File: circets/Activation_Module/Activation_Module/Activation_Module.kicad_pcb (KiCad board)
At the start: 2 copper layers, 50 parts, among them J1 Bus_Connector, J2 To_Bus, J3 From_Bus, J4 Mode_R, J5 Mode_W, J6 Enable Connector, SW1 SW_DIP_x04, SW2 SW_DIP_x04, U1 74HC541, U10 74HC541, U11 74HC00, U12 74HC541, U13 74HC541, U14 74HC541, U15 74LS86, U16 74LS86, U17 74LS32, U18 74LS32, U19 74157, U2 74HC541, U20 74157, U3 74LS86, U4 74LS86, U5 74LS32, U6 74LS32, U7 74HC541, U8 74HC541, U9 74HC00

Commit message: Started Creating Activation Module PCB
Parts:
- removed J3: From_Bus, Connector_PinHeader_2.54mm:PinHeader_1x16_P2.54mm_Vertical
- removed J4: Mode_R, Connector_PinSocket_2.54mm:PinSocket_1x03_P2.54mm_Vertical
- removed J5: Mode_W, Connector_PinSocket_2.54mm:PinSocket_1x03_P2.54mm_Vertical
- removed J6: Enable Connector, Connector_PinSocket_2.54mm:PinSocket_1x03_P2.54mm_Vertical
- added C7: 0.1µF, Capacitor_THT:C_Disc_D6.0mm_W2.5mm_P5.00mm, F.Cu at (-340.9, 76.1)
- added C8: 0.1µF, Capacitor_THT:C_Disc_D6.0mm_W2.5mm_P5.00mm, F.Cu at (-389.8, 80.2)
- added U21: 74157, Package_DIP:DIP-16_W7.62mm_Socket, F.Cu at (-318.4, 29.6)
- added U22: 74LS32, Package_DIP:DIP-14_W7.62mm_Socket, F.Cu at (-294.9, 29.6)
- added U23: 74LS00, Package_DIP:DIP-14_W7.62mm_Socket, F.Cu at (-365.4, 56.7)
- J1: footprint Computer_Component_Library:BusConnector -> Computer_Component_Library:PinSocket_1x78_P2.00mm_Horizontal
- J2: value To_Bus -> Conn_01x03_Male; footprint Connector_PinHeader_2.54mm:PinHeader_1x16_P2.54mm_Vertical -> Connector_PinSocket_2.00mm:PinSocket_1x03_P2.00mm_Vertical
- R10, R9: value 220 -> 1k
- R5, R6: value 1k -> 220
- U1, U10, U14, U8: footprint Computer_Component_Library:74HC541-PDIP -> Package_DIP:DIP-20_W7.62mm_Socket
- U11, U9: value 74HC00 -> 74HC541; footprint Package_DIP:DIP-14_W7.62mm_Socket -> Package_DIP:DIP-20_W7.62mm_Socket
- U12, U13: value 74HC541 -> 74LS86; footprint Computer_Component_Library:74HC541-PDIP -> Package_DIP:DIP-14_W7.62mm_Socket
- U15, U16: value 74LS86 -> 74LS32
- U17: value 74LS32 -> 74HC541; footprint Package_DIP:DIP-14_W7.62mm_Socket -> Package_DIP:DIP-20_W7.62mm_Socket
- U18: value 74LS32 -> 74HC00
- U19: value 74157 -> 74LS08; footprint Package_DIP:DIP-16_W7.62mm_Socket -> Package_DIP:DIP-14_W7.62mm_Socket
- U2: value 74HC541 -> AM-Connector; footprint Computer_Component_Library:74HC541-PDIP -> Computer_Component_Library:PinSocket_1x42_P2.00mm_Horizontal
- U3: value 74LS86 -> 74HC541; footprint Package_DIP:DIP-14_W7.62mm_Socket -> Package_DIP:DIP-20_W7.62mm_Socket
- U5: value 74LS32 -> 74LS86
- U7: value 74HC541 -> 74LS32; footprint Computer_Component_Library:74HC541-PDIP -> Package_DIP:DIP-14_W7.62mm_Socket
- moved C6 577.0 mm to (-349.0, 76.1), turned to 0 degrees
- moved R9 520.7 mm to (-377.1, 90.8), turned to 0 degrees
- moved R10 517.4 mm to (-370.9, 90.8), turned to 0 degrees
- moved R11 514.8 mm to (-364.8, 90.8), turned to 0 degrees
- moved D2 511.7 mm to (-377.2, 81.4)
- moved R12 509.4 mm to (-351.1, 80.2), turned to 0 degrees
- moved D4 508.1 mm to (-364.2, 81.4)
- moved D3 506.1 mm to (-370.7, 81.4)
- moved U15 505.3 mm to (-400.7, 56.7), turned to 0 degrees
- moved C3 496.6 mm to (-373.5, 76.1)
- moved C4 489.6 mm to (-365.3, 76.1), turned to 0 degrees
- moved D1 488.1 mm to (-357.7, 81.4)
- moved U16 484.5 mm to (-377.7, 33.6), turned to 0 degrees
- moved C5 477.0 mm to (-357.2, 76.1), turned to 0 degrees
- moved U4 466.7 mm to (-353.7, 56.7), turned to 0 degrees
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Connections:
- D1 pad 1: Net-(D1-Pad1) -> /~WE1
- D2 pad 1: Net-(D2-Pad1) -> /~WE2
- D3 pad 1: Net-(D3-Pad1) -> /~RE1
- D4 pad 1: Net-(D4-Pad1) -> /~RE2
- J1 pad 37: Net-(J1-Pad37) -> /WE1:0
- J1 pad 38: Net-(J1-Pad38) -> /WE1:1
- J1 pad 39: Net-(J1-Pad39) -> /WE1:2
- J1 pad 40: Net-(J1-Pad40) -> /WE1:3
- J1 pad 41: Net-(J1-Pad41) -> /WE1:4
- J1 pad 42: Net-(J1-Pad42) -> /WE1:5
- J1 pad 43: Net-(J1-Pad43) -> /WE1:6
- J1 pad 44: Net-(J1-Pad44) -> /WE2:0
- J1 pad 45: Net-(J1-Pad45) -> /WE2:1
- J1 pad 46: Net-(J1-Pad46) -> /WE2:2
- J1 pad 47: Net-(J1-Pad47) -> /WE2:3
- J1 pad 48: Net-(J1-Pad48) -> /WE2:4
- J1 pad 49: Net-(J1-Pad49) -> /WE2:5
- J1 pad 50: Net-(J1-Pad50) -> /WE2:6
- J1 pad 51: Net-(J1-Pad51) -> /RE1:0
- J1 pad 52: Net-(J1-Pad52) -> /RE1:1
- J1 pad 53: Net-(J1-Pad53) -> /RE1:2
- J1 pad 54: Net-(J1-Pad54) -> /RE1:3
- J1 pad 55: Net-(J1-Pad55) -> /RE1:4
- J1 pad 56: Net-(J1-Pad56) -> /RE1:5
- J1 pad 57: Net-(J1-Pad57) -> /RE1:6
- J1 pad 58: Net-(J1-Pad58) -> /RE2:0
- J1 pad 59: Net-(J1-Pad59) -> /RE2:1
- J1 pad 60: Net-(J1-Pad60) -> /RE2:2
- J1 pad 61: Net-(J1-Pad61) -> /RE2:3
- J1 pad 62: Net-(J1-Pad62) -> /RE2:4
- J1 pad 63: Net-(J1-Pad63) -> /RE2:5
- J1 pad 64: Net-(J1-Pad64) -> /RE2:6
- J1 pad 65: (no net) -> Net-(J1-Pad65)
- J1 pad 66: (no net) -> Net-(J1-Pad66)
- J1 pad 67: (no net) -> Net-(J1-Pad67)
- J2 pad 2: Net-(J2-Pad2) -> /~SUP
- J2 pad 3: Net-(J2-Pad3) -> GND
- R10 pad 1: +5V -> GND
- R10 pad 2: Net-(D2-Pad2) -> Net-(R10-Pad2)
- R5 pad 1: GND -> +5V
- R5 pad 2: Net-(R5-Pad2) -> Net-(D1-Pad2)
- R6 pad 1: GND -> +5V
- R6 pad 2: Net-(R6-Pad2) -> Net-(D2-Pad2)
- R9 pad 1: +5V -> GND
- R9 pad 2: Net-(D1-Pad2) -> Net-(R9-Pad2)
- SW2 pad 5: Net-(R8-Pad2) -> Net-(R10-Pad2)
- SW2 pad 6: Net-(R7-Pad2) -> Net-(R9-Pad2)
- SW2 pad 7: Net-(R6-Pad2) -> Net-(R8-Pad2)
- SW2 pad 8: Net-(R5-Pad2) -> Net-(R7-Pad2)
- U1 pad 1: Net-(D3-Pad1) -> /~RE1
- U1 pad 2: Net-(J2-Pad1) -> Net-(U1-Pad2)
- U1 pad 3: Net-(J2-Pad2) -> Net-(U1-Pad3)
- U1 pad 4: Net-(J2-Pad3) -> Net-(U1-Pad4)
- U1 pad 5: Net-(J2-Pad4) -> Net-(U1-Pad5)
- U1 pad 6: Net-(J2-Pad5) -> Net-(U1-Pad6)
- U1 pad 7: Net-(J2-Pad6) -> Net-(U1-Pad7)
- U1 pad 8: Net-(J2-Pad7) -> Net-(U1-Pad8)
- U1 pad 9: Net-(J2-Pad8) -> Net-(U1-Pad9)
- U10 pad 1: Net-(D4-Pad1) -> /~RE2
- U10 pad 2: Net-(J2-Pad1) -> Net-(U1-Pad2)
- U10 pad 3: Net-(J2-Pad2) -> Net-(U1-Pad3)
- U10 pad 4: Net-(J2-Pad3) -> Net-(U1-Pad4)
- U10 pad 5: Net-(J2-Pad4) -> Net-(U1-Pad5)
- U10 pad 6: Net-(J2-Pad5) -> Net-(U1-Pad6)
- U10 pad 7: Net-(J2-Pad6) -> Net-(U1-Pad7)
- U10 pad 8: Net-(J2-Pad7) -> Net-(U1-Pad8)
- U10 pad 9: Net-(J2-Pad8) -> Net-(U1-Pad9)
- U11 pad 1: Net-(U11-Pad1) -> /~RE2
- U11 pad 10: Net-(U11-Pad10) -> GND
- U11 pad 11: Net-(U11-Pad11) -> Net-(J1-Pad36)
- U11 pad 12: Net-(U11-Pad12) -> Net-(J1-Pad35)
- U11 pad 13: Net-(U11-Pad13) -> Net-(J1-Pad34)
- U11 pad 14: +5V -> Net-(J1-Pad33)
- U11 pad 2: Net-(U11-Pad1) -> Net-(U11-Pad2)
- U11 pad 7: GND -> Net-(U11-Pad7)
- U12 pad 1: Net-(D4-Pad1) -> Net-(R7-Pad2)
- U12 pad 10: GND -> /RE1:5
- U12 pad 11: Net-(J1-Pad36) -> Net-(U12-Pad11)
- U12 pad 12: Net-(J1-Pad35) -> Net-(R10-Pad2)
- U12 pad 13: Net-(J1-Pad34) -> /RE1:6
- U12 pad 14: Net-(J1-Pad33) -> +5V
- U12 pad 2: Net-(J2-Pad9) -> /RE1:3
- U12 pad 3: Net-(J2-Pad10) -> Net-(U12-Pad3)
- U12 pad 4: Net-(J2-Pad11) -> Net-(R8-Pad2)
- U12 pad 5: Net-(J2-Pad12) -> /RE1:4
- U12 pad 6: Net-(J2-Pad13) -> Net-(U12-Pad6)
- U12 pad 7: Net-(J2-Pad14) -> GND
- U12 pad 8: Net-(J2-Pad15) -> Net-(U12-Pad8)
- U12 pad 9: Net-(J2-Pad16) -> Net-(R9-Pad2)
- U13 pad 1: GND -> Net-(R7-Pad2)
- U13 pad 10: GND -> /RE2:5
- U13 pad 11: Net-(J3-Pad8) -> Net-(U13-Pad11)
- U13 pad 12: Net-(J3-Pad7) -> Net-(R10-Pad2)
- U13 pad 13: Net-(J3-Pad6) -> /RE2:6
- U13 pad 14: Net-(J3-Pad5) -> +5V
- U13 pad 2: Net-(J1-Pad21) -> /RE2:3
- U13 pad 3: Net-(J1-Pad22) -> Net-(U13-Pad3)
- U13 pad 4: Net-(J1-Pad23) -> Net-(R8-Pad2)
- U13 pad 5: Net-(J1-Pad24) -> /RE2:4
- U13 pad 6: Net-(J1-Pad25) -> Net-(U13-Pad6)
- U13 pad 7: Net-(J1-Pad26) -> GND
- U13 pad 8: Net-(J1-Pad27) -> Net-(U13-Pad8)
- U13 pad 9: Net-(J1-Pad28) -> Net-(R9-Pad2)
- U14 pad 11: Net-(J3-Pad16) -> Net-(U14-Pad11)
- U14 pad 12: Net-(J3-Pad15) -> Net-(U14-Pad12)
- U14 pad 13: Net-(J3-Pad14) -> Net-(U14-Pad13)
- U14 pad 14: Net-(J3-Pad13) -> Net-(U14-Pad14)
- U14 pad 15: Net-(J3-Pad12) -> Net-(U14-Pad15)
- U14 pad 16: Net-(J3-Pad11) -> Net-(U14-Pad16)
- U14 pad 17: Net-(J3-Pad10) -> Net-(U14-Pad17)
- U14 pad 18: Net-(J3-Pad9) -> Net-(U14-Pad18)
- U14 pad 19: Net-(D2-Pad1) -> /~WE2
- U14 pad 2: Net-(J1-Pad29) -> Net-(J1-Pad21)
- U14 pad 3: Net-(J1-Pad30) -> Net-(J1-Pad22)
- U14 pad 4: Net-(J1-Pad31) -> Net-(J1-Pad23)
- U14 pad 5: Net-(J1-Pad32) -> Net-(J1-Pad24)
- U14 pad 6: Net-(J1-Pad33) -> Net-(J1-Pad25)
- U14 pad 7: Net-(J1-Pad34) -> Net-(J1-Pad26)
- U14 pad 8: Net-(J1-Pad35) -> Net-(J1-Pad27)
- U14 pad 9: Net-(J1-Pad36) -> Net-(J1-Pad28)
- U15 pad 1: Net-(R5-Pad2) -> Net-(U12-Pad3)
- U15 pad 10: Net-(J1-Pad56) -> Net-(U15-Pad10)
- U15 pad 11: Net-(U15-Pad11) -> (no net)
- U15 pad 12: Net-(R8-Pad2) -> (no net)
- U15 pad 13: Net-(J1-Pad57) -> (no net)
- U15 pad 2: Net-(J1-Pad54) -> Net-(U12-Pad6)
- U15 pad 4: Net-(R6-Pad2) -> Net-(U13-Pad8)
- U15 pad 5: Net-(J1-Pad55) -> Net-(U13-Pad11)
- U15 pad 6: Net-(U15-Pad6) -> Net-(U15-Pad10)
- U15 pad 9: Net-(R7-Pad2) -> Net-(U15-Pad9)
- U16 pad 1: Net-(R5-Pad2) -> Net-(U13-Pad3)
- U16 pad 10: Net-(J1-Pad49) -> Net-(U12-Pad11)
- U16 pad 11: Net-(U16-Pad11) -> (no net)
- U16 pad 12: Net-(R8-Pad2) -> (no net)
- U16 pad 13: Net-(J1-Pad50) -> (no net)
- U16 pad 2: Net-(J1-Pad47) -> Net-(U13-Pad6)
- U16 pad 3: Net-(U16-Pad3) -> Net-(U15-Pad9)
- U16 pad 4: Net-(R6-Pad2) -> Net-(U15-Pad3)
- U16 pad 5: Net-(J1-Pad48) -> Net-(U16-Pad5)
- U16 pad 8: Net-(U16-Pad8) -> Net-(U16-Pad5)
- U16 pad 9: Net-(R7-Pad2) -> Net-(U12-Pad8)
- U17 pad 1: Net-(U16-Pad3) -> GND
- U17 pad 10: Net-(U17-Pad10) -> GND
- U17 pad 14: +5V -> Net-(U17-Pad14)
- U17 pad 2: Net-(U16-Pad6) -> Net-(J1-Pad29)
- U17 pad 3: Net-(U17-Pad3) -> Net-(J1-Pad30)
- U17 pad 4: Net-(U16-Pad8) -> Net-(J1-Pad31)
- U17 pad 5: Net-(U16-Pad11) -> Net-(J1-Pad32)
- U17 pad 6: Net-(U17-Pad10) -> Net-(J1-Pad33)
- U17 pad 7: GND -> Net-(J1-Pad34)
- U17 pad 8: Net-(D4-Pad1) -> Net-(J1-Pad35)
- U17 pad 9: Net-(U17-Pad3) -> Net-(J1-Pad36)
- U18 pad 1: Net-(U15-Pad3) -> Net-(U18-Pad1)
- U18 pad 10: Net-(U15-Pad11) -> Net-(U18-Pad10)
- U18 pad 11: /RE -> (no net)
- U18 pad 12: Net-(D3-Pad1) -> (no net)
- U18 pad 13: Net-(D4-Pad1) -> (no net)
- U18 pad 2: Net-(U15-Pad6) -> Net-(U18-Pad1)
- U18 pad 4: Net-(U18-Pad3) -> (no net)
- U18 pad 5: Net-(U15-Pad8) -> (no net)
- U18 pad 6: Net-(U18-Pad6) -> (no net)
- U18 pad 8: Net-(D3-Pad1) -> Net-(U18-Pad8)
- U18 pad 9: Net-(U18-Pad6) -> Net-(U18-Pad10)
- U19 pad 1: Net-(D3-Pad1) -> Net-(U18-Pad3)
- U19 pad 10: Net-(U19-Pad10) -> (no net)
- U19 pad 11: Net-(U19-Pad11) -> (no net)
- U19 pad 12: Net-(J4-Pad3) -> (no net)
- U19 pad 13: Net-(J1-Pad46) -> (no net)
- U19 pad 14: Net-(J1-Pad60) -> GND
- U19 pad 2: Net-(J1-Pad58) -> Net-(J1-Pad4)
- U19 pad 3: Net-(J1-Pad44) -> /WE_F
- U19 pad 4: Net-(J4-Pad1) -> Net-(U18-Pad3)
- U19 pad 5: Net-(J1-Pad59) -> Net-(J1-Pad3)
- U19 pad 6: Net-(J1-Pad45) -> /WE_R
- U19 pad 7: Net-(J4-Pad2) -> +5V
- U19 pad 8: GND -> (no net)
- U19 pad 9: Net-(U19-Pad9) -> (no net)
- U2 pad 1: Net-(D3-Pad1) -> Net-(U2-Pad1)
- U2 pad 10: GND -> Net-(U18-Pad8)
- U2 pad 11: Net-(J1-Pad20) -> Net-(U14-Pad18)
- U2 pad 12: Net-(J1-Pad19) -> Net-(U14-Pad17)
- U2 pad 13: Net-(J1-Pad18) -> Net-(U14-Pad16)
- U2 pad 14: Net-(J1-Pad17) -> Net-(U14-Pad15)
- U2 pad 15: Net-(J1-Pad16) -> Net-(U14-Pad14)
- U2 pad 16: Net-(J1-Pad15) -> Net-(U14-Pad13)
- U2 pad 17: Net-(J1-Pad14) -> Net-(U14-Pad12)
- U2 pad 18: Net-(J1-Pad13) -> Net-(U14-Pad11)
- U2 pad 19: GND -> Net-(U17-Pad18)
- U2 pad 2: Net-(J2-Pad9) -> Net-(U2-Pad2)
- U2 pad 20: +5V -> Net-(U17-Pad17)
- U2 pad 3: Net-(J2-Pad10) -> Net-(U2-Pad3)
- U2 pad 4: Net-(J2-Pad11) -> Net-(U2-Pad4)
- U2 pad 5: Net-(J2-Pad12) -> Net-(U2-Pad5)
- U2 pad 6: Net-(J2-Pad13) -> Net-(U2-Pad6)
- U2 pad 7: Net-(J2-Pad14) -> /WE_R
- U2 pad 8: Net-(J2-Pad15) -> /WE_F
- U2 pad 9: Net-(J2-Pad16) -> Net-(U18-Pad3)
- U20 pad 1: Net-(D1-Pad1) -> /~RE1
- U20 pad 12: Net-(J5-Pad3) -> Net-(U2-Pad3)
- U20 pad 13: Net-(J1-Pad53) -> /RE2:2
- U20 pad 14: Net-(J1-Pad39) -> /RE1:2
- U20 pad 2: Net-(J1-Pad37) -> /RE1:0
- U20 pad 3: Net-(J1-Pad51) -> /RE2:0
- U20 pad 4: Net-(J5-Pad1) -> Net-(U2-Pad1)
- U20 pad 5: Net-(J1-Pad38) -> /RE1:1
- U20 pad 6: Net-(J1-Pad52) -> /RE2:1
- U20 pad 7: Net-(J5-Pad2) -> Net-(U2-Pad2)
- U3 pad 1: Net-(R1-Pad2) -> /~RE1
- U3 pad 10: Net-(J1-Pad42) -> GND
- U3 pad 11: Net-(U3-Pad11) -> Net-(J1-Pad20)
- U3 pad 12: Net-(R4-Pad2) -> Net-(J1-Pad19)
- U3 pad 13: Net-(J1-Pad43) -> Net-(J1-Pad18)
- U3 pad 14: GND -> Net-(J1-Pad17)
- U3 pad 2: Net-(J1-Pad40) -> Net-(U11-Pad2)
- U3 pad 3: Net-(U3-Pad3) -> Net-(U11-Pad3)
- U3 pad 4: Net-(R2-Pad2) -> Net-(U11-Pad4)
- U3 pad 5: Net-(J1-Pad41) -> Net-(U11-Pad5)
- U3 pad 6: Net-(U3-Pad6) -> Net-(U11-Pad6)
- U3 pad 7: +5V -> Net-(U11-Pad7)
- U3 pad 8: Net-(U3-Pad8) -> Net-(U11-Pad8)
- U3 pad 9: Net-(R3-Pad2) -> Net-(U11-Pad9)
- U4 pad 10: Net-(J1-Pad63) -> /WE1:5
- U4 pad 13: Net-(J1-Pad64) -> /WE1:6
- U4 pad 14: +5V -> GND
- U4 pad 2: Net-(J1-Pad61) -> /WE1:3
- U4 pad 5: Net-(J1-Pad62) -> /WE1:4
- U4 pad 7: GND -> +5V
- U5 pad 1: Net-(U3-Pad3) -> Net-(R1-Pad2)
- U5 pad 10: Net-(U3-Pad11) -> /WE2:5
- U5 pad 11: Net-(U11-Pad1) -> Net-(U5-Pad11)
- U5 pad 12: Net-(D1-Pad1) -> Net-(R4-Pad2)
- U5 pad 13: Net-(D2-Pad1) -> /WE2:6
- U5 pad 2: Net-(U3-Pad6) -> /WE2:3
- U5 pad 4: Net-(U5-Pad3) -> Net-(R2-Pad2)
- U5 pad 5: Net-(U3-Pad8) -> /WE2:4
- U5 pad 8: Net-(D1-Pad1) -> Net-(U5-Pad8)
- U5 pad 9: Net-(U5-Pad6) -> Net-(R3-Pad2)
- U6 pad 11: Net-(U6-Pad11) -> Net-(U18-Pad1)
- U6 pad 12: Net-(U6-Pad12) -> /~WE1
- U6 pad 13: Net-(U6-Pad13) -> /~WE2
- U6 pad 4: Net-(U4-Pad8) -> Net-(U5-Pad8)
- U6 pad 5: Net-(U4-Pad11) -> Net-(U5-Pad11)
- U6 pad 8: Net-(D2-Pad1) -> Net-(U22-Pad1)
- U6 pad 9: Net-(U6-Pad3) -> Net-(U6-Pad9)
- U7 pad 1: GND -> Net-(U5-Pad3)
- U7 pad 10: GND -> Net-(U4-Pad11)
- U7 pad 11: Net-(J3-Pad8) -> Net-(U18-Pad10)
- U7 pad 12: Net-(J3-Pad7) -> /~RE1
- U7 pad 13: Net-(J3-Pad6) -> /~RE2
- U7 pad 14: Net-(J3-Pad5) -> +5V
- U7 pad 2: Net-(J1-Pad5) -> Net-(U5-Pad6)
- U7 pad 3: Net-(J1-Pad6) -> Net-(U6-Pad9)
- U7 pad 4: Net-(J1-Pad7) -> Net-(U6-Pad3)
- U7 pad 5: Net-(J1-Pad8) -> Net-(U7-Pad5)
- U7 pad 6: Net-(J1-Pad9) -> Net-(U22-Pad4)
- U7 pad 7: Net-(J1-Pad10) -> GND
- U7 pad 8: Net-(J1-Pad11) -> Net-(U7-Pad5)
- U7 pad 9: Net-(J1-Pad12) -> Net-(U4-Pad8)
- U8 pad 11: Net-(J3-Pad16) -> Net-(U14-Pad11)
- U8 pad 12: Net-(J3-Pad15) -> Net-(U14-Pad12)
- U8 pad 13: Net-(J3-Pad14) -> Net-(U14-Pad13)
- U8 pad 14: Net-(J3-Pad13) -> Net-(U14-Pad14)
- U8 pad 15: Net-(J3-Pad12) -> Net-(U14-Pad15)
- U8 pad 16: Net-(J3-Pad11) -> Net-(U14-Pad16)
- U8 pad 17: Net-(J3-Pad10) -> Net-(U14-Pad17)
- U8 pad 18: Net-(J3-Pad9) -> Net-(U14-Pad18)
- U8 pad 19: Net-(D1-Pad1) -> /~WE1
- U8 pad 2: Net-(J1-Pad13) -> Net-(J1-Pad5)
- U8 pad 3: Net-(J1-Pad14) -> Net-(J1-Pad6)
- U8 pad 4: Net-(J1-Pad15) -> Net-(J1-Pad7)
- U8 pad 5: Net-(J1-Pad16) -> Net-(J1-Pad8)
- U8 pad 6: Net-(J1-Pad17) -> Net-(J1-Pad9)
- U8 pad 7: Net-(J1-Pad18) -> Net-(J1-Pad10)
- U8 pad 8: Net-(J1-Pad19) -> Net-(J1-Pad11)
- U8 pad 9: Net-(J1-Pad20) -> Net-(J1-Pad12)
- U9 pad 1: Net-(U11-Pad3) -> GND
- U9 pad 10: Net-(J1-Pad3) -> GND
- U9 pad 11: /WE_R -> Net-(U17-Pad11)
- U9 pad 12: Net-(U9-Pad12) -> Net-(U17-Pad12)
- U9 pad 13: Net-(U9-Pad12) -> Net-(U17-Pad13)
- U9 pad 14: GND -> Net-(U17-Pad14)
- U9 pad 2: Net-(J1-Pad4) -> Net-(J1-Pad13)
- U9 pad 3: Net-(U9-Pad3) -> Net-(J1-Pad14)
- U9 pad 4: Net-(U9-Pad3) -> Net-(J1-Pad15)
- U9 pad 5: Net-(U9-Pad3) -> Net-(J1-Pad16)
- U9 pad 6: /WE_F -> Net-(J1-Pad17)
- U9 pad 7: +5V -> Net-(J1-Pad18)
- U9 pad 8: Net-(U9-Pad12) -> Net-(J1-Pad19)
- U9 pad 9: Net-(U11-Pad3) -> Net-(J1-Pad20)
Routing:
- net Net-(J1-Pad13): track 35.2 -> 433.0 mm, vias 0 -> 2
- net Net-(J1-Pad14): track 35.2 -> 424.9 mm, vias 0 -> 2
- net Net-(J1-Pad15): track 35.2 -> 415.7 mm, vias 0 -> 2
- net Net-(J1-Pad16): track 35.2 -> 407.1 mm, vias 0 -> 2
- net Net-(J1-Pad17): track 35.2 -> 399.1 mm, vias 0 -> 2
- net Net-(J1-Pad18): track 35.2 -> 390.0 mm, vias 0 -> 2
- net Net-(J1-Pad19): track 35.2 -> 382.3 mm, vias 0 -> 2
- net Net-(J1-Pad20): track 35.2 -> 371.7 mm, vias 0 -> 2
- net Net-(U1-Pad2): track 0.00 -> 311.0 mm, vias 0 -> 1
- net Net-(J1-Pad29): track 50.2 -> 360.9 mm, vias 0 -> 2
- net Net-(U1-Pad3): track 0.00 -> 308.6 mm, vias 0 -> 1
- net Net-(U1-Pad4): track 0.00 -> 306.5 mm, vias 0 -> 1
- net Net-(U1-Pad5): track 0.00 -> 303.6 mm, vias 0 -> 1
- net Net-(U1-Pad6): track 0.00 -> 302.2 mm, vias 0 -> 1
- net Net-(U1-Pad7): track 0.00 -> 299.5 mm, vias 0 -> 1
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
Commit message: Update Kicad to version 6 (and all of the schematics)
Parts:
- moved D3 790.1 mm to (387.1, 305.2)
- moved J2 783.9 mm to (370.1, 304.0)
- moved SW2 781.8 mm to (356.8, 270.2)
- moved R9 781.1 mm to (367.8, 325.8)
- moved D2 778.2 mm to (361.2, 327.1)
- moved D4 777.6 mm to (380.6, 305.2)
- moved D1 765.2 mm to (374.1, 305.2)
- moved C8 751.8 mm to (328.9, 301.1)
- moved SW1 749.9 mm to (368.2, 270.2)
- moved R6 748.4 mm to (342.7, 312.0)
- moved R5 748.4 mm to (336.6, 312.0)
- moved R11 747.1 mm to (348.9, 312.0)
- moved C3 746.1 mm to (337.0, 304.0)
- moved C4 746.1 mm to (345.1, 304.0)
- moved C5 746.1 mm to (353.3, 304.0)
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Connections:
- net /~RE1 renamed /~{RE1}
- net /~RE2 renamed /~{RE2}
- net /~SUP renamed /~{SUP}
- net /~WE1 renamed /~{WE1}
- net /~WE2 renamed /~{WE2}
- J1 pad 66: Net-(J1-Pad66) -> unconnected-(J1-Pad66)
- J1 pad 67: Net-(J1-Pad67) -> unconnected-(J1-Pad67)
- U20 pad 10: Net-(U20-Pad10) -> unconnected-(U20-Pad10)
- U20 pad 11: Net-(U20-Pad11) -> unconnected-(U20-Pad11)
- U20 pad 9: Net-(U20-Pad9) -> unconnected-(U20-Pad9)
- U21 pad 10: Net-(U21-Pad10) -> unconnected-(U21-Pad10)
- U21 pad 11: Net-(U21-Pad11) -> unconnected-(U21-Pad11)
- U21 pad 9: Net-(U21-Pad9) -> unconnected-(U21-Pad9)
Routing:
- net Net-(J1-Pad20): track 371.7 -> 0.00 mm, vias 2 -> 0
- net Net-(U1-Pad2): track 311.0 -> 78.9 mm
- net Net-(U1-Pad3): track 308.6 -> 77.9 mm
- net Net-(U1-Pad6): track 302.2 -> 71.6 mm
- net Net-(U1-Pad4): track 306.5 -> 76.8 mm
- net Net-(U1-Pad5): track 303.6 -> 74.7 mm
- net Net-(U1-Pad7): track 299.5 -> 72.5 mm
- net Net-(U1-Pad9): track 291.8 -> 67.9 mm
- net Net-(U1-Pad8): track 295.1 -> 71.4 mm
- net Net-(J1-Pad12): track 120.8 -> 285.0 mm, vias 1 -> 2
- net +5V: track 246.0 -> 400.4 mm, vias 0 -> 1
- net Net-(J1-Pad36): track 297.4 -> 143.7 mm, vias 2 -> 0
- net Net-(J1-Pad35): track 307.0 -> 154.2 mm, vias 2 -> 0
- net Net-(J1-Pad33): track 325.8 -> 173.8 mm, vias 2 -> 0
- net Net-(J1-Pad34): track 316.2 -> 164.4 mm, vias 2 -> 0
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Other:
- net class Default removed

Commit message: Futher Advanced Progress in build PCB Layout for AM
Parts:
- U10, U14, U3, U9: moved to B.Cu
- moved U19 268.1 mm to (409.7, 30.9)
- moved U18 268.1 mm to (408.7, 50.9)
- moved C2 201.9 mm to (482.8, 206.5)
- moved C4 200.0 mm to (514.7, 198.0)
- moved R11 200.0 mm to (518.4, 206.0)
- moved R12 200.0 mm to (524.6, 206.0)
- moved R5 200.0 mm to (506.2, 206.0)
- moved C1 200.0 mm to (490.3, 195.1)
- moved C3 200.0 mm to (506.6, 198.0)
- moved C5 200.0 mm to (522.9, 198.0)
- moved C6 200.0 mm to (531.0, 198.0)
- moved C8 200.0 mm to (498.4, 195.1)
- moved D1 200.0 mm to (543.6, 199.3)
- moved D3 200.0 mm to (556.6, 199.3)
- moved D4 200.0 mm to (550.1, 199.3)
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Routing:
- net /RE1:0: track 0.00 -> 357.1 mm, vias 0 -> 2
- net /RE2:0: track 0.00 -> 352.4 mm, vias 0 -> 2
- net /RE1:1: track 0.00 -> 348.8 mm, vias 0 -> 3
- net /RE1:2: track 0.00 -> 348.6 mm, vias 0 -> 2
- net /RE2:1: track 0.00 -> 347.5 mm, vias 0 -> 1
- net /WE1:2: track 0.00 -> 344.9 mm, vias 0 -> 2
- net /RE2:2: track 0.00 -> 338.2 mm, vias 0 -> 1
- net /WE1:0: track 0.00 -> 337.4 mm, vias 0 -> 1
- net /WE2:2: track 0.00 -> 335.5 mm
- net /WE1:1: track 0.00 -> 333.6 mm, vias 0 -> 1
- net /WE2:0: track 0.00 -> 328.2 mm, vias 0 -> 1
- net /WE2:1: track 0.00 -> 323.0 mm, vias 0 -> 1
- net GND: track 416.0 -> 710.1 mm, vias 3 -> 4
- net /WE1:6: track 0.00 -> 291.5 mm
- net Net-(J1-Pad21): track 123.4 -> 409.3 mm
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
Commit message: RedesignedPCB Layout for Activation Module
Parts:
- removed U23: 74LS00, Package_DIP:DIP-14_W7.62mm_Socket
- U1, U11, U17, U8: footprint Package_DIP:DIP-20_W7.62mm_Socket -> Package_SO:SO-20_12.8x7.5mm_P1.27mm
- U10, U14, U3, U9: footprint Package_DIP:DIP-20_W7.62mm_Socket -> Package_SO:SO-20_12.8x7.5mm_P1.27mm; moved to F.Cu
- moved C5 479.8 mm to (47.3, 134.2), turned to 90 degrees
- moved D3 463.9 mm to (108.2, 80.5), turned to 180 degrees
- moved D1 456.6 mm to (102.7, 80.5), turned to 180 degrees
- moved D4 452.3 mm to (113.7, 80.5), turned to 180 degrees
- moved C2 450.3 mm to (39.2, 129.1), turned to -90 degrees
- moved C6 447.5 mm to (83.9, 178.6), turned to 90 degrees
- moved C3 441.7 mm to (99.2, 27.4), turned to 180 degrees
- moved D2 435.0 mm to (119.2, 80.5), turned to 180 degrees
- moved R12 434.7 mm to (111.0, 72.0), turned to -90 degrees
- moved C7 434.4 mm to (94.3, 20.5)
- moved R11 433.7 mm to (106.0, 72.0), turned to -90 degrees
- moved R5 426.3 mm to (101.5, 71.9), turned to -90 degrees
- moved R6 418.3 mm to (116.0, 72.0), turned to -90 degrees
- moved J2 417.0 mm to (124.8, 155.7), turned to 180 degrees
- moved C8 402.9 mm to (124.3, 45.6), turned to -90 degrees
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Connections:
- U18 pad 4: (no net) -> Net-(J1-Pad65)
- U18 pad 5: (no net) -> Net-(J1-Pad65)
- U18 pad 6: (no net) -> Net-(J2-Pad1)
- U22 pad 14: GND -> +5V
- U22 pad 7: +5V -> GND
- U4 pad 14: GND -> +5V
- U4 pad 7: +5V -> GND
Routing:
- net /~{WE1}: track 0.00 -> 310.9 mm, vias 0 -> 13
- net Net-(J1-Pad21): track 409.3 -> 127.9 mm, vias 1 -> 4
- net Net-(J1-Pad5): track 370.0 -> 104.6 mm, vias 0 -> 1
- net Net-(J1-Pad22): track 399.5 -> 135.8 mm, vias 1 -> 4
- net /~{WE2}: track 0.00 -> 261.7 mm, vias 0 -> 12
- net /RE1:2: track 348.6 -> 95.2 mm, vias 2 -> 4
- net /RE1:1: track 348.8 -> 97.0 mm, vias 3 -> 1
- net Net-(J1-Pad6): track 359.9 -> 109.2 mm, vias 0 -> 1
- net /RE1:0: track 357.1 -> 109.0 mm, vias 2 -> 5
- net Net-(J1-Pad23): track 389.4 -> 142.4 mm, vias 1 -> 4
- net /RE2:1: track 347.5 -> 103.1 mm, vias 1 -> 0
- net /RE2:0: track 352.4 -> 108.3 mm
- net /~{RE2}: track 0.00 -> 239.4 mm, vias 0 -> 13
- net Net-(J1-Pad65): track 0.00 -> 236.9 mm, vias 0 -> 11
- net Net-(J1-Pad7): track 349.9 -> 114.4 mm, vias 0 -> 1
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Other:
- board outline added: 101.5 x 177 mm

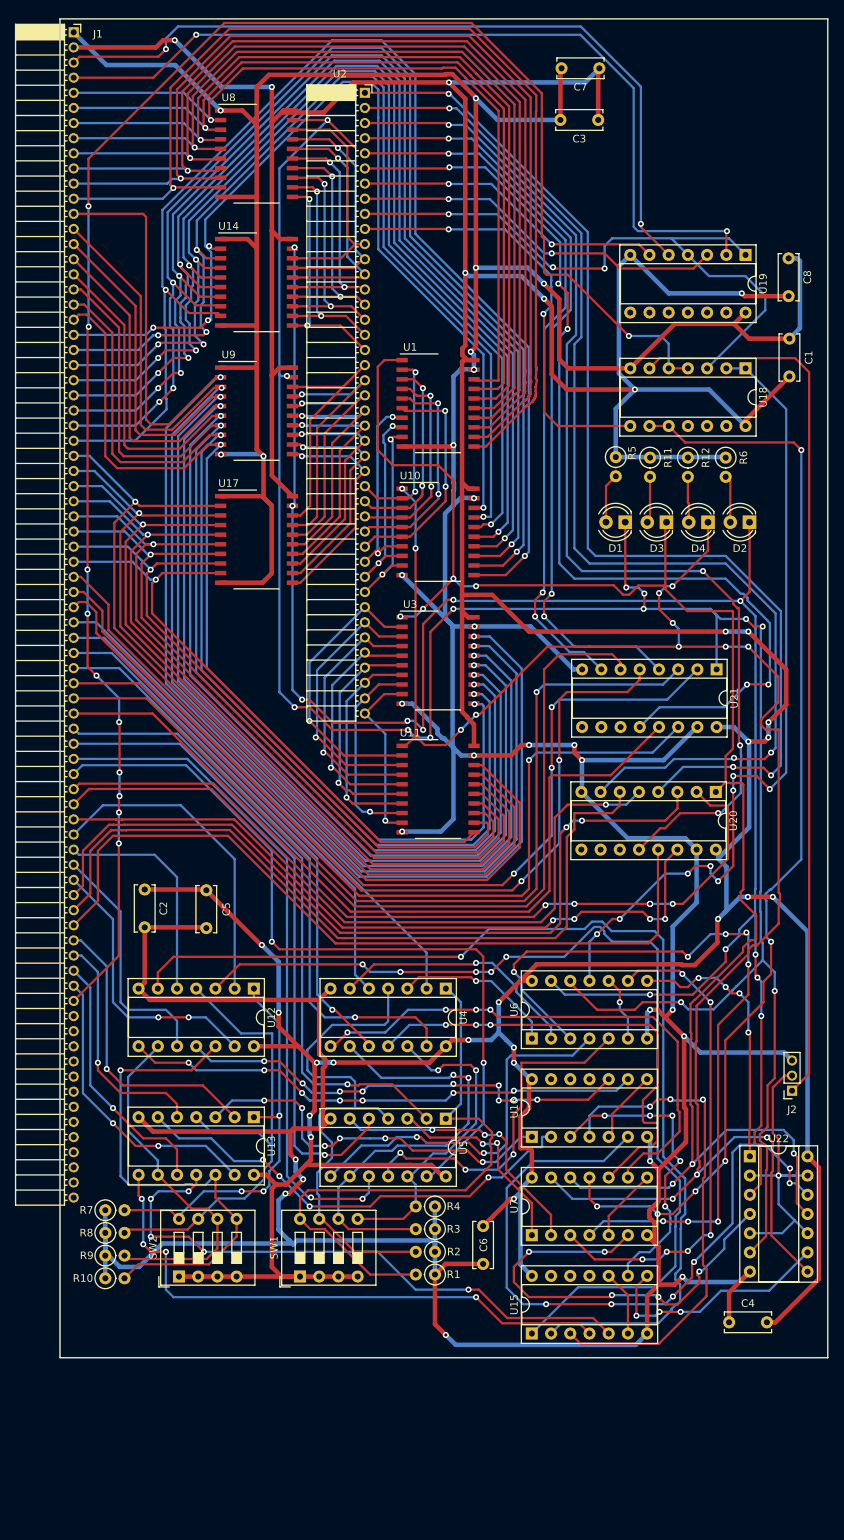
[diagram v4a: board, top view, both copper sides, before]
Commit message: Added gerber files to Activation Module and corrected PinHeader
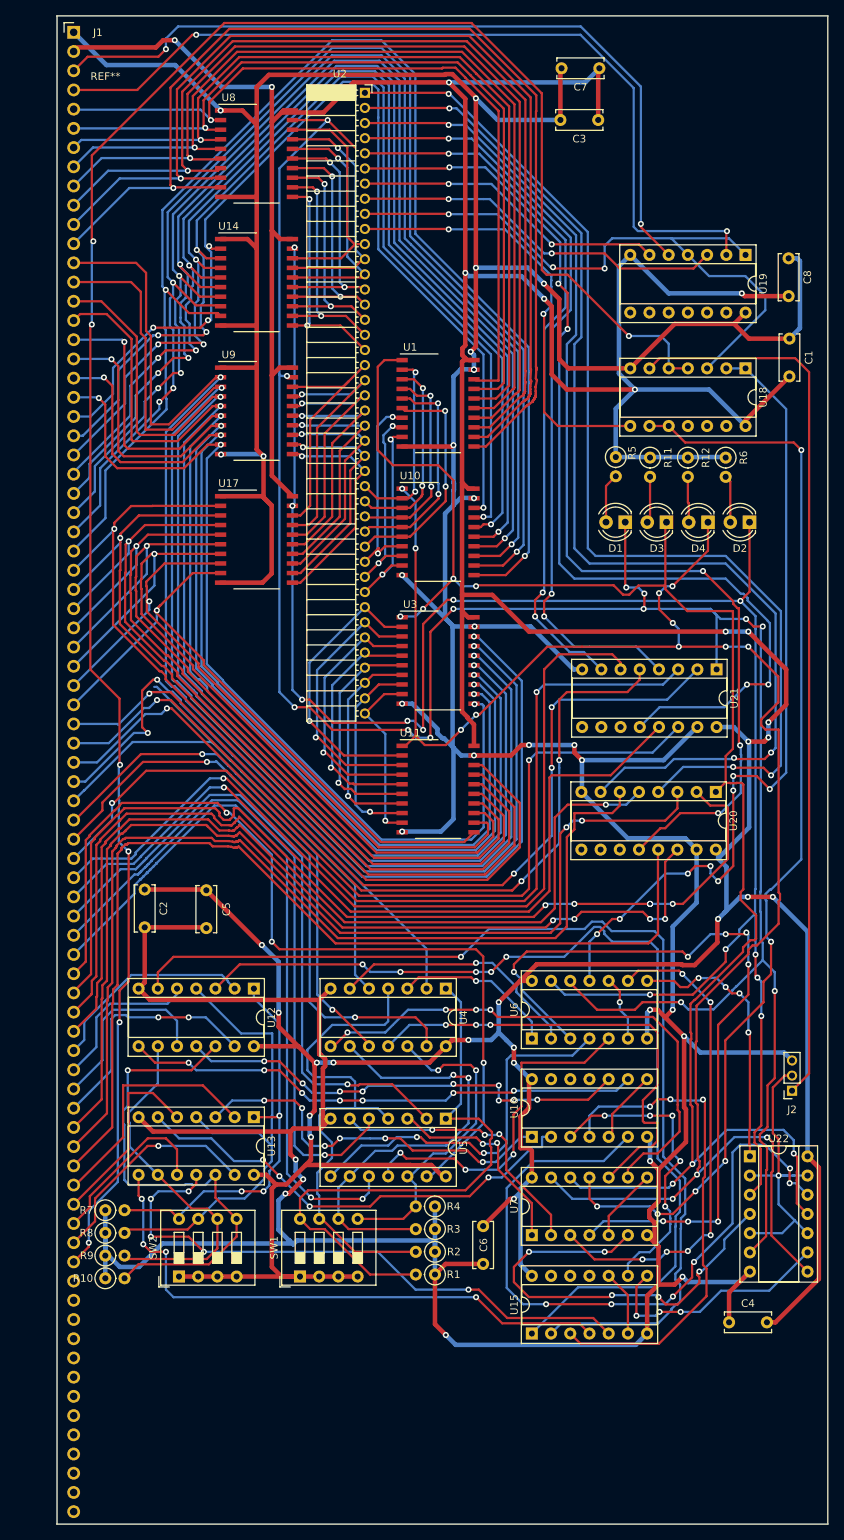
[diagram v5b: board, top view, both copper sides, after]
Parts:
- J1: footprint Computer_Component_Library:PinSocket_1x78_P2.00mm_Horizontal -> Computer_Component_Library:PinHeader_1x78_P2.54mm_Horizontal
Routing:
- net Net-(J1-Pad65): track 236.9 -> 272.4 mm, vias 11 -> 7
- net /RE2:0: track 108.3 -> 137.7 mm
- net /RE2:2: track 103.6 -> 133.1 mm
- net /RE2:1: track 103.1 -> 132.0 mm
- net /RE1:2: track 95.2 -> 119.7 mm
- net /RE1:1: track 97.0 -> 118.2 mm
- net /RE1:0: track 109.0 -> 130.0 mm
- net /WE2:6: track 104.9 -> 121.0 mm, vias 2 -> 3
- net /RE1:3: track 43.0 -> 27.6 mm
- net /RE2:5: track 34.4 -> 23.1 mm, vias 1 -> 0
- net Net-(J1-Pad20): track 133.4 -> 122.8 mm, vias 2 -> 3
- net Net-(J1-Pad28): track 171.9 -> 181.7 mm
- net /RE2:6: track 39.2 -> 29.9 mm, vias 2 -> 1
- net Net-(J1-Pad27): track 165.2 -> 174.4 mm
- net /RE1:4: track 29.9 -> 20.8 mm
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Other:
- board size 101.5 x 177 mm -> 101.9 x 199.4 mm
